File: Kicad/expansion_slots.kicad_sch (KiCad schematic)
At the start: 8 parts, among them J1301 Conn_01x09, J1302 Neotron-Expansion-Slot, J1303 Conn_01x09, J1304 Conn_01x09, J1305 Neotron-Expansion-Slot, J1306 Conn_01x06, J1307 Neotron-Expansion-Slot, J1308 Neotron-Expansion-Slot

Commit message: Reworked audio circuit.
Based on TLV320AIC23B evaluation board. Removed Pi filters. Used SMD
electrolytic caps for headphone out.
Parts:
- renumbered J1306 to J1301, J1305 to J1303, J1307 to J1304, J1308 to J1305, J1301 to J1306, J1303 to J1307, J1304 to J1308
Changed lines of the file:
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@@
   (symbol (lib_id "power:+5V") (at 260.35 99.695 0) (unit 1)
     (in_bom yes) (on_board yes)
-    (property "Reference" "#PWR01321" (id 0) (at 260.35 103.505 0)
+    (property "Reference" "#PWR01305" (id 0) (at 260.35 103.505 0)
       (effects (font (size 1.27 1.27)) hide)
     )
@@
   (symbol (lib_name "Neotron-Expansion-Slot_3") (lib_id "Neotron-Common-Hardware:Neotron-Expansion-Slot") (at 121.285 105.41 0) (unit 1)
     (in_bom yes) (on_board yes)
-    (property "Reference" "J1305" (id 0) (at 120.65 87.249 0))
+    (property "Reference" "J1303" (id 0) (at 120.65 87.249 0))
     (property "Value" "Neotron-Expansion-Slot" (id 1) (at 120.65 89.5604 0))
     (property "Footprint" "Neotron-Common-Hardware:Neotron-Expansion-Slot" (id 2) (at 132.715 95.25 0)
@@
   (symbol (lib_name "Neotron-Expansion-Slot_2") (lib_id "Neotron-Common-Hardware:Neotron-Expansion-Slot") (at 179.705 105.41 0) (unit 1)
     (in_bom yes) (on_board yes)
-    (property "Reference" "J1307" (id 0) (at 179.07 87.249 0))
+    (property "Reference" "J1304" (id 0) (at 179.07 87.249 0))
     (property "Value" "Neotron-Expansion-Slot" (id 1) (at 179.07 89.5604 0))
     (property "Footprint" "Neotron-Common-Hardware:Neotron-Expansion-Slot" (id 2) (at 191.135 95.25 0)
@@
   (symbol (lib_id "power:GND") (at 257.81 122.555 0) (unit 1)
     (in_bom yes) (on_board yes)
-    (property "Reference" "#PWR01320" (id 0) (at 257.81 128.905 0)
+    (property "Reference" "#PWR01317" (id 0) (at 257.81 128.905 0)
       (effects (font (size 1.27 1.27)) hide)
     )
@@
   (symbol (lib_id "power:GND") (at 40.64 122.555 0) (unit 1)
     (in_bom yes) (on_board yes)
-    (property "Reference" "#PWR01304" (id 0) (at 40.64 128.905 0)
+    (property "Reference" "#PWR01310" (id 0) (at 40.64 128.905 0)
       (effects (font (size 1.27 1.27)) hide)
     )
@@
   (symbol (lib_id "power:GND") (at 147.955 67.31 0) (unit 1)
     (in_bom yes) (on_board yes)
-    (property "Reference" "#PWR01314" (id 0) (at 147.955 73.66 0)
+    (property "Reference" "#PWR01301" (id 0) (at 147.955 73.66 0)
       (effects (font (size 1.27 1.27)) hide)
     )
@@
   (symbol (lib_id "power:GND") (at 77.47 122.555 0) (unit 1)
     (in_bom yes) (on_board yes)
-    (property "Reference" "#PWR01307" (id 0) (at 77.47 128.905 0)
+    (property "Reference" "#PWR01311" (id 0) (at 77.47 128.905 0)
       (effects (font (size 1.27 1.27)) hide)
     )
@@
   (symbol (lib_id "Connector_Generic:Conn_01x09") (at 78.74 175.26 0) (mirror x) (unit 1)
     (in_bom yes) (on_board yes)
-    (property "Reference" "J1304" (id 0) (at 76.2 159.385 0)
+    (property "Reference" "J1308" (id 0) (at 76.2 159.385 0)
       (effects (font (size 1.27 1.27)) (justify left))
     )
@@
   (symbol (lib_id "power:GND") (at 71.755 186.055 0) (unit 1)
     (in_bom yes) (on_board yes)
-    (property "Reference" "#PWR01306" (id 0) (at 71.755 192.405 0)
+    (property "Reference" "#PWR01322" (id 0) (at 71.755 192.405 0)
       (effects (font (size 1.27 1.27)) hide)
     )
@@
   (symbol (lib_id "power:+3V3") (at 264.16 104.14 0) (unit 1)
     (in_bom yes) (on_board yes)
-    (property "Reference" "#PWR01322" (id 0) (at 264.16 107.95 0)
+    (property "Reference" "#PWR01309" (id 0) (at 264.16 107.95 0)
       (effects (font (size 1.27 1.27)) hide)
     )
@@
   (symbol (lib_id "power:+3V3") (at 27.178 162.56 0) (unit 1)
     (in_bom yes) (on_board yes)
-    (property "Reference" "#PWR01301" (id 0) (at 27.178 166.37 0)
+    (property "Reference" "#PWR01318" (id 0) (at 27.178 166.37 0)
       (effects (font (size 1.27 1.27)) hide)
     )
@@
   (symbol (lib_id "power:+5V") (at 32.385 162.56 0) (unit 1)
     (in_bom yes) (on_board yes)
-    (property "Reference" "#PWR01302" (id 0) (at 32.385 166.37 0)
+    (property "Reference" "#PWR01319" (id 0) (at 32.385 166.37 0)
       (effects (font (size 1.27 1.27)) hide)
     )
@@
   (symbol (lib_id "power:GND") (at 52.705 186.055 0) (unit 1)
     (in_bom yes) (on_board yes)
-    (property "Reference" "#PWR01305" (id 0) (at 52.705 192.405 0)
+    (property "Reference" "#PWR01321" (id 0) (at 52.705 192.405 0)
       (effects (font (size 1.27 1.27)) hide)
     )
@@
   (symbol (lib_id "power:+3V3") (at 203.835 104.14 0) (unit 1)
     (in_bom yes) (on_board yes)
-    (property "Reference" "#PWR01318" (id 0) (at 203.835 107.95 0)
+    (property "Reference" "#PWR01308" (id 0) (at 203.835 107.95 0)
       (effects (font (size 1.27 1.27)) hide)
     )
@@
   (symbol (lib_id "Connector_Generic:Conn_01x09") (at 60.96 175.26 0) (mirror x) (unit 1)
     (in_bom yes) (on_board yes)
-    (property "Reference" "J1303" (id 0) (at 58.42 159.385 0)
+    (property "Reference" "J1307" (id 0) (at 58.42 159.385 0)
       (effects (font (size 1.27 1.27)) (justify left))
     )
@@
   (symbol (lib_id "power:GND") (at 220.98 122.555 0) (unit 1)
     (in_bom yes) (on_board yes)
-    (property "Reference" "#PWR01319" (id 0) (at 220.98 128.905 0)
+    (property "Reference" "#PWR01316" (id 0) (at 220.98 128.905 0)
       (effects (font (size 1.27 1.27)) hide)
     )
@@
   (symbol (lib_id "power:GND") (at 32.385 186.055 0) (unit 1)
     (in_bom yes) (on_board yes)
-    (property "Reference" "#PWR01303" (id 0) (at 32.385 192.405 0)
+    (property "Reference" "#PWR01320" (id 0) (at 32.385 192.405 0)
       (effects (font (size 1.27 1.27)) hide)
     )
@@
   (symbol (lib_id "power:+5V") (at 80.01 99.695 0) (unit 1)
     (in_bom yes) (on_board yes)
-    (property "Reference" "#PWR01308" (id 0) (at 80.01 103.505 0)
+    (property "Reference" "#PWR01302" (id 0) (at 80.01 103.505 0)
       (effects (font (size 1.27 1.27)) hide)
     )
@@
   (symbol (lib_id "power:+5V") (at 141.605 99.695 0) (unit 1)
     (in_bom yes) (on_board yes)
-    (property "Reference" "#PWR01312" (id 0) (at 141.605 103.505 0)
+    (property "Reference" "#PWR01303" (id 0) (at 141.605 103.505 0)
       (effects (font (size 1.27 1.27)) hide)
     )
@@
   (symbol (lib_id "power:+5V") (at 200.025 99.695 0) (unit 1)
     (in_bom yes) (on_board yes)
-    (property "Reference" "#PWR01317" (id 0) (at 200.025 103.505 0)
+    (property "Reference" "#PWR01304" (id 0) (at 200.025 103.505 0)
       (effects (font (size 1.27 1.27)) hide)
     )
@@
   (symbol (lib_id "power:+3V3") (at 145.415 104.14 0) (unit 1)
     (in_bom yes) (on_board yes)
-    (property "Reference" "#PWR01313" (id 0) (at 145.415 107.95 0)
+    (property "Reference" "#PWR01307" (id 0) (at 145.415 107.95 0)
       (effects (font (size 1.27 1.27)) hide)
     )
@@
   (symbol (lib_id "power:GND") (at 195.58 122.555 0) (unit 1)
     (in_bom yes) (on_board yes)
-    (property "Reference" "#PWR01316" (id 0) (at 195.58 128.905 0)
+    (property "Reference" "#PWR01315" (id 0) (at 195.58 128.905 0)
       (effects (font (size 1.27 1.27)) hide)
     )
@@
   (symbol (lib_id "power:GND") (at 160.655 122.555 0) (unit 1)
     (in_bom yes) (on_board yes)
-    (property "Reference" "#PWR01315" (id 0) (at 160.655 128.905 0)
+    (property "Reference" "#PWR01314" (id 0) (at 160.655 128.905 0)
       (effects (font (size 1.27 1.27)) hide)
     )
@@
   (symbol (lib_name "Neotron-Expansion-Slot_1") (lib_id "Neotron-Common-Hardware:Neotron-Expansion-Slot") (at 240.03 105.41 0) (unit 1)
     (in_bom yes) (on_board yes)
-    (property "Reference" "J1308" (id 0) (at 239.395 87.249 0))
+    (property "Reference" "J1305" (id 0) (at 239.395 87.249 0))
     (property "Value" "Neotron-Expansion-Slot" (id 1) (at 239.395 89.5604 0))
     (property "Footprint" "Neotron-Common-Hardware:Neotron-Expansion-Slot" (id 2) (at 251.46 95.25 0)
@@
   (symbol (lib_id "Connector_Generic:Conn_01x09") (at 40.64 175.26 0) (mirror x) (unit 1)
     (in_bom yes) (on_board yes)
-    (property "Reference" "J1301" (id 0) (at 38.1 159.385 0)
+    (property "Reference" "J1306" (id 0) (at 38.1 159.385 0)
       (effects (font (size 1.27 1.27)) (justify left))
     )
@@
   (symbol (lib_id "power:+3V3") (at 83.82 104.14 0) (unit 1)
     (in_bom yes) (on_board yes)
-    (property "Reference" "#PWR01309" (id 0) (at 83.82 107.95 0)
+    (property "Reference" "#PWR01306" (id 0) (at 83.82 107.95 0)
       (effects (font (size 1.27 1.27)) hide)
     )
@@
   (symbol (lib_id "power:GND") (at 137.16 122.555 0) (unit 1)
     (in_bom yes) (on_board yes)
-    (property "Reference" "#PWR01311" (id 0) (at 137.16 128.905 0)
+    (property "Reference" "#PWR01313" (id 0) (at 137.16 128.905 0)
       (effects (font (size 1.27 1.27)) hide)
     )
@@
   (symbol (lib_id "power:GND") (at 102.235 122.555 0) (unit 1)
     (in_bom yes) (on_board yes)
-    (property "Reference" "#PWR01310" (id 0) (at 102.235 128.905 0)
+    (property "Reference" "#PWR01312" (id 0) (at 102.235 128.905 0)
       (effects (font (size 1.27 1.27)) hide)
     )
@@
   (symbol (lib_id "Connector:Conn_01x06_Male") (at 154.94 60.96 180) (unit 1)
     (in_bom yes) (on_board yes)
-    (property "Reference" "J1306" (id 0) (at 154.94 55.88 0)
+    (property "Reference" "J1301" (id 0) (at 154.94 55.88 0)
       (effects (font (size 1.27 1.27)) (justify right))
     )

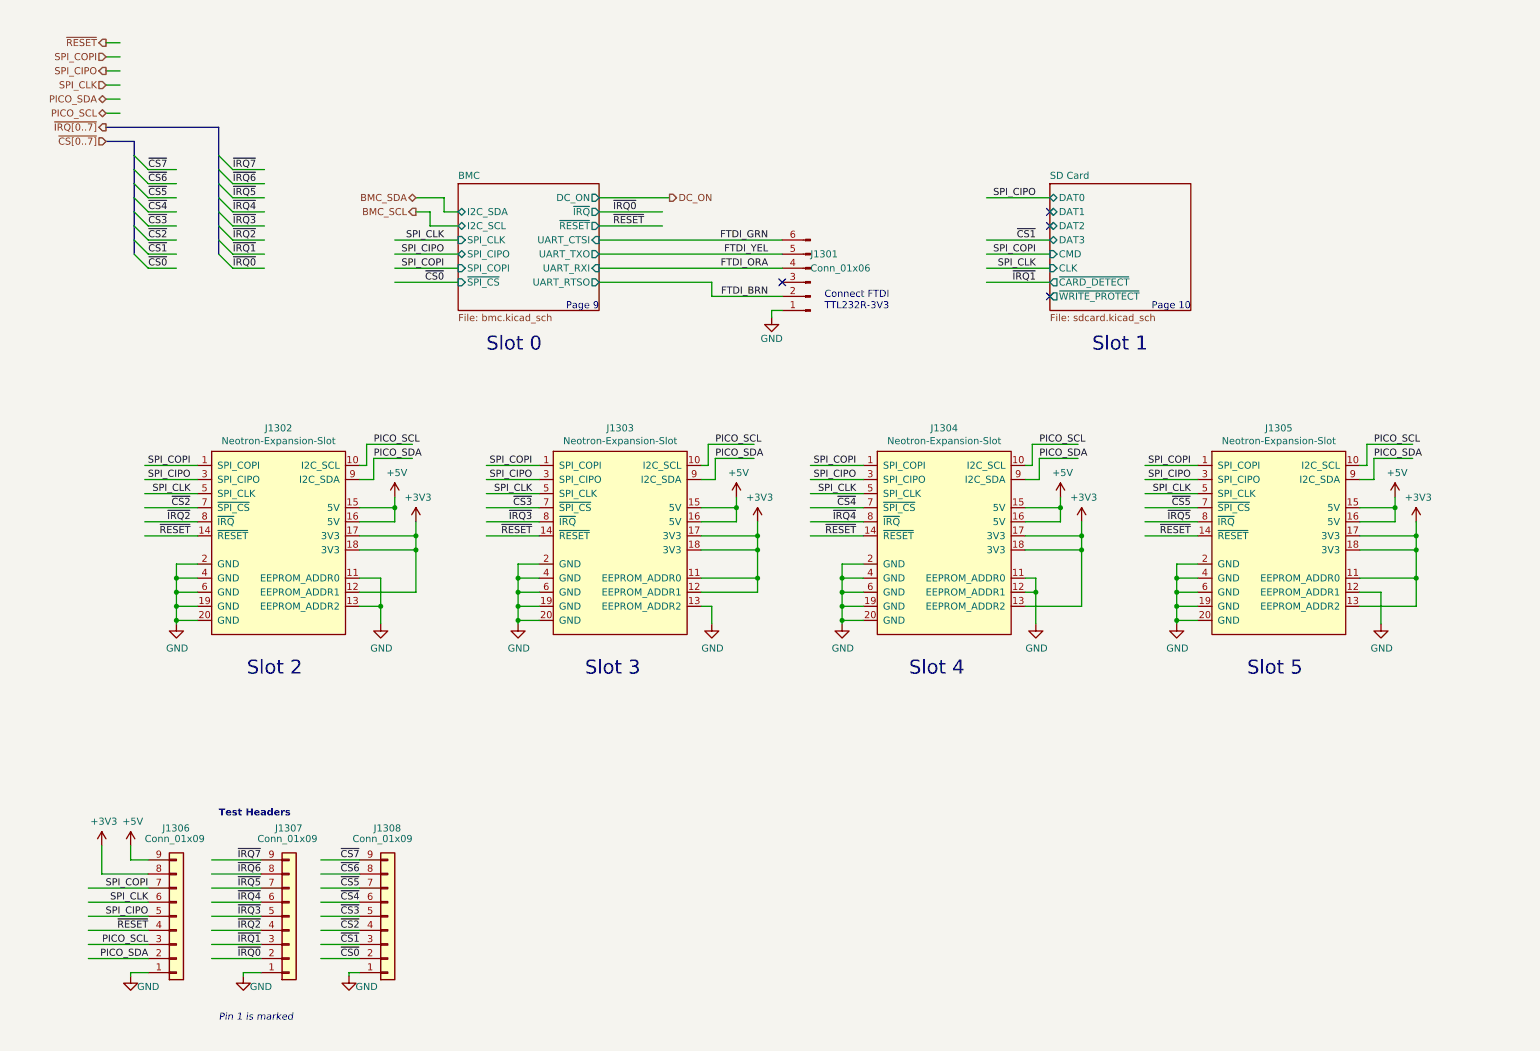
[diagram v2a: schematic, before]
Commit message: Added a PC Speaker output.
To free up a BMC pin, the HDD LED is now driven from the I/O mux.
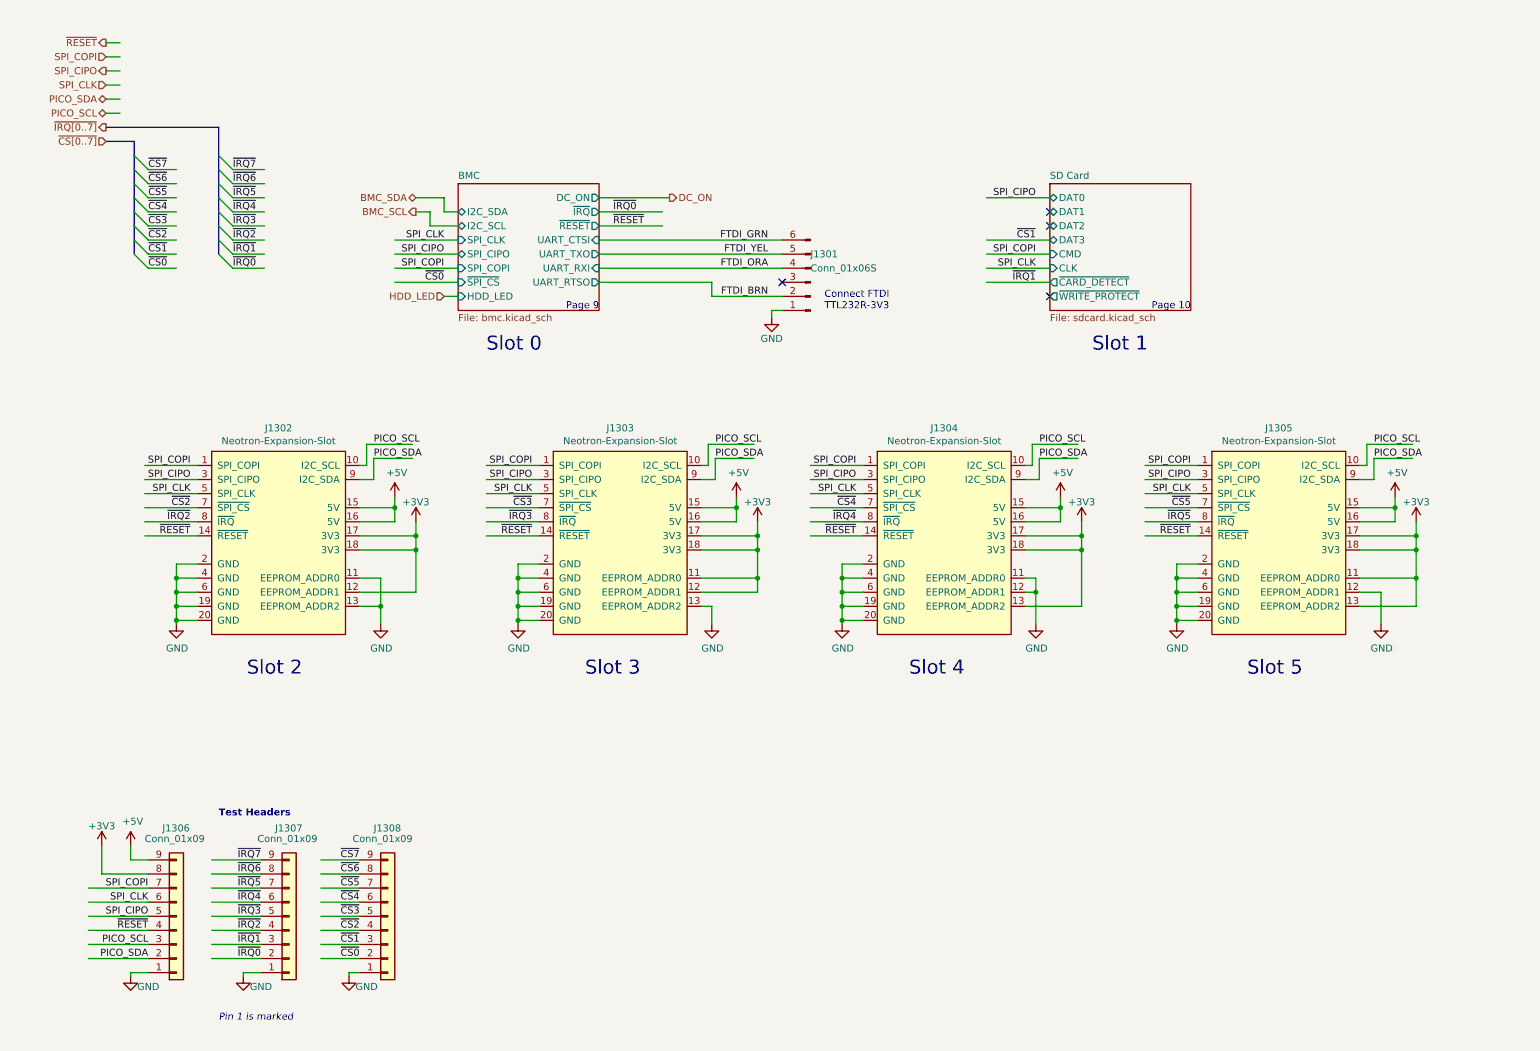
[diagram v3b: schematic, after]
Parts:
- J1301: value Conn_01x06 -> Conn_01x06S
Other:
- sheet BMC ports: added HDD_LED; removed none
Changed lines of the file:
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@@
+    (stroke (width 0) (type default) (color 0 0 0 0))
+  )
+  (wire (pts (xy 88.9 63.5) (xy 91.44 63.5))
     (stroke (width 0) (type default) (color 0 0 0 0))
   )
@@
   )
   (hierarchical_label "SPI_CIPO" (shape output) (at 27.94 22.86 180)
+    (effects (font (size 1.27 1.27)) (justify right))
+  )
+  (hierarchical_label "HDD_LED" (shape input) (at 88.9 63.5 180)
     (effects (font (size 1.27 1.27)) (justify right))
   )
@@
       (effects (font (size 1.27 1.27)) hide)
     )
-    (property "Value" "+3V3" (id 1) (at 264.541 99.7458 0))
+    (property "Value" "+3V3" (id 1) (at 264.16 100.584 0))
     (property "Footprint" "" (id 2) (at 264.16 104.14 0)
       (effects (font (size 1.27 1.27)) hide)
@@
       (effects (font (size 1.27 1.27)) hide)
     )
-    (property "Value" "+3V3" (id 1) (at 27.559 158.1658 0))
+    (property "Value" "+3V3" (id 1) (at 27.178 159.004 0))
     (property "Footprint" "" (id 2) (at 27.178 162.56 0)
       (effects (font (size 1.27 1.27)) hide)
@@
       (effects (font (size 1.27 1.27)) hide)
     )
-    (property "Value" "+3V3" (id 1) (at 204.216 99.7458 0))
+    (property "Value" "+3V3" (id 1) (at 203.835 100.584 0))
     (property "Footprint" "" (id 2) (at 203.835 104.14 0)
       (effects (font (size 1.27 1.27)) hide)
@@
       (effects (font (size 1.27 1.27)) hide)
     )
-    (property "Value" "+3V3" (id 1) (at 145.796 99.7458 0))
+    (property "Value" "+3V3" (id 1) (at 145.415 100.584 0))
     (property "Footprint" "" (id 2) (at 145.415 104.14 0)
       (effects (font (size 1.27 1.27)) hide)
@@
       (effects (font (size 1.27 1.27)) hide)
     )
-    (property "Value" "+3V3" (id 1) (at 84.201 99.7458 0))
+    (property "Value" "+3V3" (id 1) (at 83.82 100.584 0))
     (property "Footprint" "" (id 2) (at 83.82 104.14 0)
       (effects (font (size 1.27 1.27)) hide)
@@
       (effects (font (size 1.27 1.27)) (justify right))
     )
-    (property "Value" "Conn_01x06" (id 1) (at 154.94 58.42 0)
+    (property "Value" "Conn_01x06S" (id 1) (at 154.94 58.42 0)
       (effects (font (size 1.27 1.27)) (justify right))
     )
@@
       (effects (font (size 1.27 1.27)) (justify right))
     )
-  )
+    (pin "HDD_LED" input (at 91.44 63.5 180)
+      (effects (font (size 1.27 1.27)) (justify left))
+    )
+  )

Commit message: Replaced decoupling caps, and worked on PCB layout.
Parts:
- added NT1301, NT1302, NT1303, NT1304, NT1305, NT1306, NT1307, NT1308, NT1309, NT1310, NT1311, NT1312: NetTie_2, NetTie:NetTie-2_SMD_Pad0.5mm, symbol Device:NetTie_2
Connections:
- net +3V3: now also NT1302.2, NT1304.2, NT1305.2, NT1306.2, NT1311.2, NT1312.2; no longer J1302.12 (EEPROM_ADDR1), J1303.11 (EEPROM_ADDR0), J1303.12 (EEPROM_ADDR1), J1304.13 (EEPROM_ADDR2), J1305.11 (EEPROM_ADDR0), J1305.13 (EEPROM_ADDR2)
- net GND: now also NT1301.2, NT1303.2, NT1307.2, NT1308.2, NT1309.2, NT1310.2; no longer J1302.11 (EEPROM_ADDR0), J1302.13 (EEPROM_ADDR2), J1303.13 (EEPROM_ADDR2), J1304.11 (EEPROM_ADDR0), J1304.12 (EEPROM_ADDR1), J1305.12 (EEPROM_ADDR1)
- new net: J1303.11 (EEPROM_ADDR0), NT1302.1
- new net: J1303.12 (EEPROM_ADDR1), NT1306.1
- new net: J1303.13 (EEPROM_ADDR2), NT1310.1
- new net: J1304.13 (EEPROM_ADDR2), NT1311.1
- new net: J1304.11 (EEPROM_ADDR0), NT1303.1
- new net: J1304.12 (EEPROM_ADDR1), NT1307.1
- new net: J1302.11 (EEPROM_ADDR0), NT1301.1
- new net: J1305.11 (EEPROM_ADDR0), NT1304.1
- new net: J1302.13 (EEPROM_ADDR2), NT1309.1
- new net: J1305.13 (EEPROM_ADDR2), NT1312.1
- new net: J1305.12 (EEPROM_ADDR1), NT1308.1
- new net: J1302.12 (EEPROM_ADDR1), NT1305.1

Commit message: Started re-tracking. Also sets up board stack to JLCPCB 7628
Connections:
- net SPI_CIPO: now also J1306.7 (Pin_7); no longer J1306.5 (Pin_5)
- net SPI_CLK: now also J1306.5 (Pin_5); no longer J1306.6 (Pin_6)
- net SPI_COPI: now also J1306.6 (Pin_6); no longer J1306.7 (Pin_7)
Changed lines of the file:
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@@
     (effects (font (size 1.27 1.27)) (justify left bottom))
   )
-  (label "SPI_CIPO" (at 35.56 175.26 180)
+  (label "SPI_CIPO" (at 35.56 170.18 180)
     (effects (font (size 1.27 1.27)) (justify right bottom))
   )
@@
     (effects (font (size 1.27 1.27)) (justify right bottom))
   )
-  (label "SPI_COPI" (at 35.56 170.18 180)
+  (label "SPI_COPI" (at 35.56 172.72 180)
     (effects (font (size 1.27 1.27)) (justify right bottom))
   )
-  (label "SPI_CLK" (at 35.56 172.72 180)
+  (label "SPI_CLK" (at 35.56 175.26 180)
     (effects (font (size 1.27 1.27)) (justify right bottom))
   )
